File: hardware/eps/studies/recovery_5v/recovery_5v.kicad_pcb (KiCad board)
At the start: 2 copper layers, 1 part, among them U1 TI_RYQ0021A_DRAFT

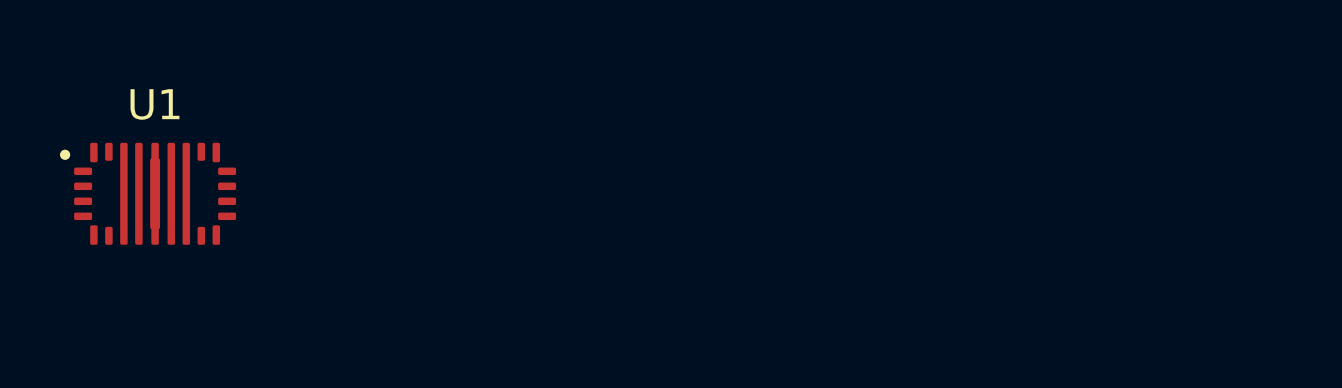
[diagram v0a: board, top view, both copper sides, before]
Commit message: Add approved Panasonic recovery bulk capacitor footprints
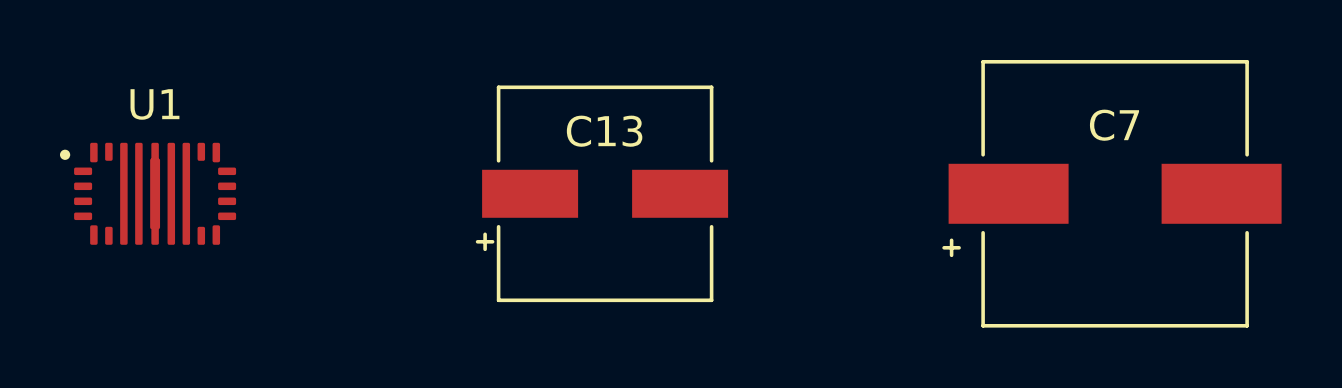
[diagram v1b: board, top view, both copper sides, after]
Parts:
- added C13: Panasonic_CP_D8_6.3x7.7mm_REVIEW, Ember_EPS_Recovery:Panasonic_CP_D8_6.3x7.7mm_REVIEW, F.Cu at (25.0, 10.0)
- added C7: Panasonic_CP_F_8x10.2mm_REVIEW, Ember_EPS_Recovery:Panasonic_CP_F_8x10.2mm_REVIEW, F.Cu at (42.0, 10.0)
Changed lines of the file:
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@@
 	  (fp_text reference "U1" (at 0.0000 -2.9500 0) (layer "F.SilkS") (effects (font (size 1 1) (thickness 0.15))))
 	  (fp_text value "TI_RYQ0021A_DRAFT" (at 0.0000 2.9500 0) (layer "F.Fab") (effects (font (size 1 1) (thickness 0.15))))
+	)
+	(footprint "Ember_EPS_Recovery:Panasonic_CP_D8_6.3x7.7mm_REVIEW"
+		(at 25 10 0)
+	  (version 20240108)
+	  (generator "konnect")
+	  (layer "F.Cu")
+	  (descr "REVIEW candidate; Panasonic D8 manufacturer recommended lands; front/component view; pad 1 positive left, pad 2 negative right; maximum component height 8 mm; approval 2026-10-23; assembly/stencil not qualified")
+	  (attr smd)
+	  (pad "1" smd rect (at -2.5 0) (size 3.2 1.6) (layers "F.Cu" "F.Paste" "F.Mask")  )
+	  (pad "2" smd rect (at 2.5 0) (size 3.2 1.6) (layers "F.Cu" "F.Paste" "F.Mask")  )
+	  (fp_rect (start -4.35 -3.65) (end 4.35 3.65) (stroke (width 0.05) (type solid)) (fill none) (layer "F.CrtYd"))
+	  (fp_line (start -3.55 -3.55) (end 3.55 -3.55) (stroke (width 0.12) (type solid)) (layer "F.SilkS"))
+	  (fp_line (start -3.55 3.55) (end 3.55 3.55) (stroke (width 0.12) (type solid)) (layer "F.SilkS"))
+	  (fp_line (start -3.55 -3.55) (end -3.55 -1.1) (stroke (width 0.12) (type solid)) (layer "F.SilkS"))
+	  (fp_line (start -3.55 1.1) (end -3.55 3.55) (stroke (width 0.12) (type solid)) (layer "F.SilkS"))
+	  (fp_line (start 3.55 -3.55) (end 3.55 -1.1) (stroke (width 0.12) (type solid)) (layer "F.SilkS"))
+	  (fp_line (start 3.55 1.1) (end 3.55 3.55) (stroke (width 0.12) (type solid)) (layer "F.SilkS"))
+	  (fp_line (start -4.25 1.6) (end -3.75 1.6) (stroke (width 0.12) (type solid)) (layer "F.SilkS"))
+	  (fp_line (start -4 1.35) (end -4 1.85) (stroke (width 0.12) (type solid)) (layer "F.SilkS"))
+	  (fp_circle (center 0 0) (end 3.15 0) (stroke (width 0.1) (type solid)) (fill none) (layer "F.Fab"))
+	  (fp_poly (pts (xy -3.3 -2.8) (xy -2.8 -3.3) (xy 3.3 -3.3) (xy 3.3 3.3) (xy -2.8 3.3) (xy -3.3 2.8)) (stroke (width 0.1) (type solid)) (fill none) (layer "F.Fab"))
+	  (fp_text reference "C13" (at 0.0000 -2.0500 0) (layer "F.SilkS") (effects (font (size 1 1) (thickness 0.15))))
+	  (fp_text value "Panasonic_CP_D8_6.3x7.7mm_REVIEW" (at 0.0000 2.0500 0) (layer "F.Fab") (effects (font (size 1 1) (thickness 0.15))))
+	)
+	(footprint "Ember_EPS_Recovery:Panasonic_CP_F_8x10.2mm_REVIEW"
+		(at 42 10 0)
+	  (version 20240108)
+	  (generator "konnect")
+	  (layer "F.Cu")
+	  (descr "REVIEW candidate; Panasonic F manufacturer recommended lands; front/component view; pad 1 positive left, pad 2 negative right; maximum component height 10.5 mm; approval 2026-10-23; assembly/stencil not qualified")
+	  (attr smd)
+	  (pad "1" smd rect (at -3.55 0) (size 4 2) (layers "F.Cu" "F.Paste" "F.Mask")  )
+	  (pad "2" smd rect (at 3.55 0) (size 4 2) (layers "F.Cu" "F.Paste" "F.Mask")  )
+	  (fp_rect (start -5.8 -4.5) (end 5.8 4.5) (stroke (width 0.05) (type solid)) (fill none) (layer "F.CrtYd"))
+	  (fp_line (start -4.4 -4.4) (end 4.4 -4.4) (stroke (width 0.12) (type solid)) (layer "F.SilkS"))
+	  (fp_line (start -4.4 4.4) (end 4.4 4.4) (stroke (width 0.12) (type solid)) (layer "F.SilkS"))
+	  (fp_line (start -4.4 -4.4) (end -4.4 -1.3) (stroke (width 0.12) (type solid)) (layer "F.SilkS"))
+	  (fp_line (start -4.4 1.3) (end -4.4 4.4) (stroke (width 0.12) (type solid)) (layer "F.SilkS"))
+	  (fp_line (start 4.4 -4.4) (end 4.4 -1.3) (stroke (width 0.12) (type solid)) (layer "F.SilkS"))
+	  (fp_line (start 4.4 1.3) (end 4.4 4.4) (stroke (width 0.12) (type solid)) (layer "F.SilkS"))
+	  (fp_line (start -5.7 1.8) (end -5.2 1.8) (stroke (width 0.12) (type solid)) (layer "F.SilkS"))
+	  (fp_line (start -5.45 1.55) (end -5.45 2.05) (stroke (width 0.12) (type solid)) (layer "F.SilkS"))
+	  (fp_circle (center 0 0) (end 4 0) (stroke (width 0.1) (type solid)) (fill none) (layer "F.Fab"))
+	  (fp_poly (pts (xy -4.15 -3.65) (xy -3.65 -4.15) (xy 4.15 -4.15) (xy 4.15 4.15) (xy -3.65 4.15) (xy -4.15 3.65)) (stroke (width 0.1) (type solid)) (fill none) (layer "F.Fab"))
+	  (fp_text reference "C7" (at 0.0000 -2.2500 0) (layer "F.SilkS") (effects (font (size 1 1) (thickness 0.15))))
+	  (fp_text value "Panasonic_CP_F_8x10.2mm_REVIEW" (at 0.0000 2.2500 0) (layer "F.Fab") (effects (font (size 1 1) (thickness 0.15))))
 	))
